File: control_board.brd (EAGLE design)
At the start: 190 x 180 mm, 132 parts, among them J17 JST_PH_B3B-PH-K-S(LF)(SN), J18 JST_PH_B3B-PH-K-S(LF)(SN), J19 JST_PH_B3B-PH-K-S(LF)(SN), J20 JST_PH_B3B-PH-K-S(LF)(SN), J21 JST_PH_B3B-PH-K-S(LF)(SN), J22 JST_PH_B3B-PH-K-S(LF)(SN), J23 JST_PH_B3B-PH-K-S(LF)(SN), J24 JST_PH_B3B-PH-K-S(LF)(SN), J25 JST_PH_B3B-PH-K-S(LF)(SN), J26 JST_PH_B3B-PH-K-S(LF)(SN), J27 JST_PH_B3B-PH-K-S(LF)(SN), J28 JST_PH_B3B-PH-K-S(LF)(SN), J29 JST_PH_B3B-PH-K-S(LF)(SN), J30 JST_PH_B3B-PH-K-S(LF)(SN), J31 JST_PH_B3B-PH-K-S(LF)(SN), J32 JST_PH_B3B-PH-K-S(LF)(SN), U18 AD7730BRUZ, U19 AD5360BSTZ, U20 ADR425ARZ, U21 AD7730BRUZ, U23 AD7730BRUZ, U24 AD7730BRUZ, U25 AD7730BRUZ, U26 AD7730BRUZ, U27 AD7730BRUZ, U28 AD7730BRUZ, U4 ADR421ARZ, U5 AD7616BSTZ, X1 22-23-2031, Y1 KC2520B-C1, Y3 KC2520B-C1

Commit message: rev 0.1
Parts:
- moved JP2 0.65 mm to (138.9, 1.30)
- moved JP3 0.65 mm to (22.1, 1.30)
- moved JP4 0.65 mm to (68.9, 1.30)
- moved JP6 0.65 mm to (5.85, 1.30)
- moved JP7 0.65 mm to (52.6, 1.30)
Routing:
- net DAC2_9: track 45.2 -> 45.8 mm
- net DAC2_8: track 46.5 -> 47.1 mm
- net DAC2_7: track 54.2 -> 54.9 mm
- net DAC2_6: track 50.8 -> 51.5 mm
- net DAC2_15: track 38.4 -> 39.1 mm
- net DAC2_1: track 41.0 -> 41.6 mm
- net ADC2_5: track 41.6 -> 42.2 mm
- net ADC2_10: track 57.2 -> 57.9 mm
- net DAC2_5: track 46.9 -> 47.5 mm
- net DAC2_4: track 43.4 -> 44.1 mm
- net DAC2_3: track 41.8 -> 42.5 mm
- net DAC2_2: track 40.7 -> 41.3 mm
- net DAC2_14: track 38.3 -> 38.9 mm
- net DAC2_13: track 39.6 -> 40.3 mm
- net DAC2_12: track 40.9 -> 41.6 mm
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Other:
- board text added: "Controller Board Hitzmann 2020"

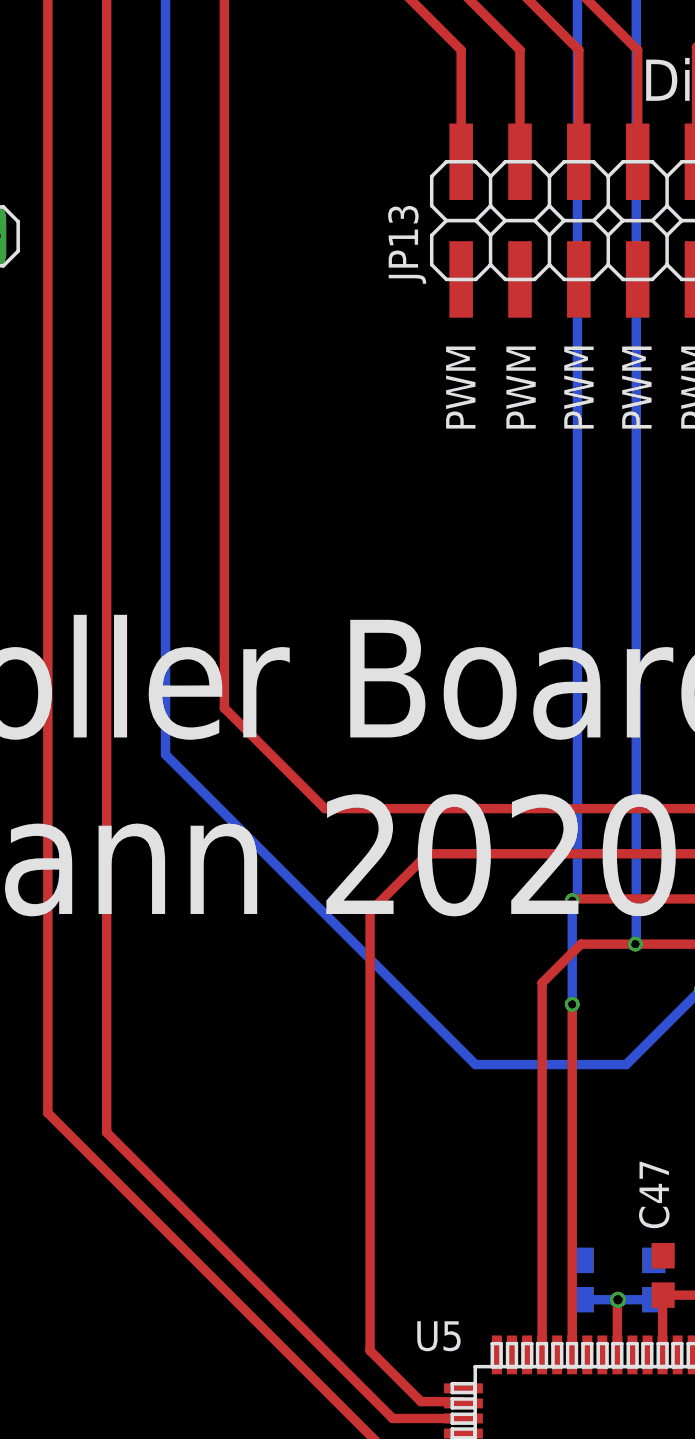
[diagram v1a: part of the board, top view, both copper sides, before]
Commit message: added GND to Teensy
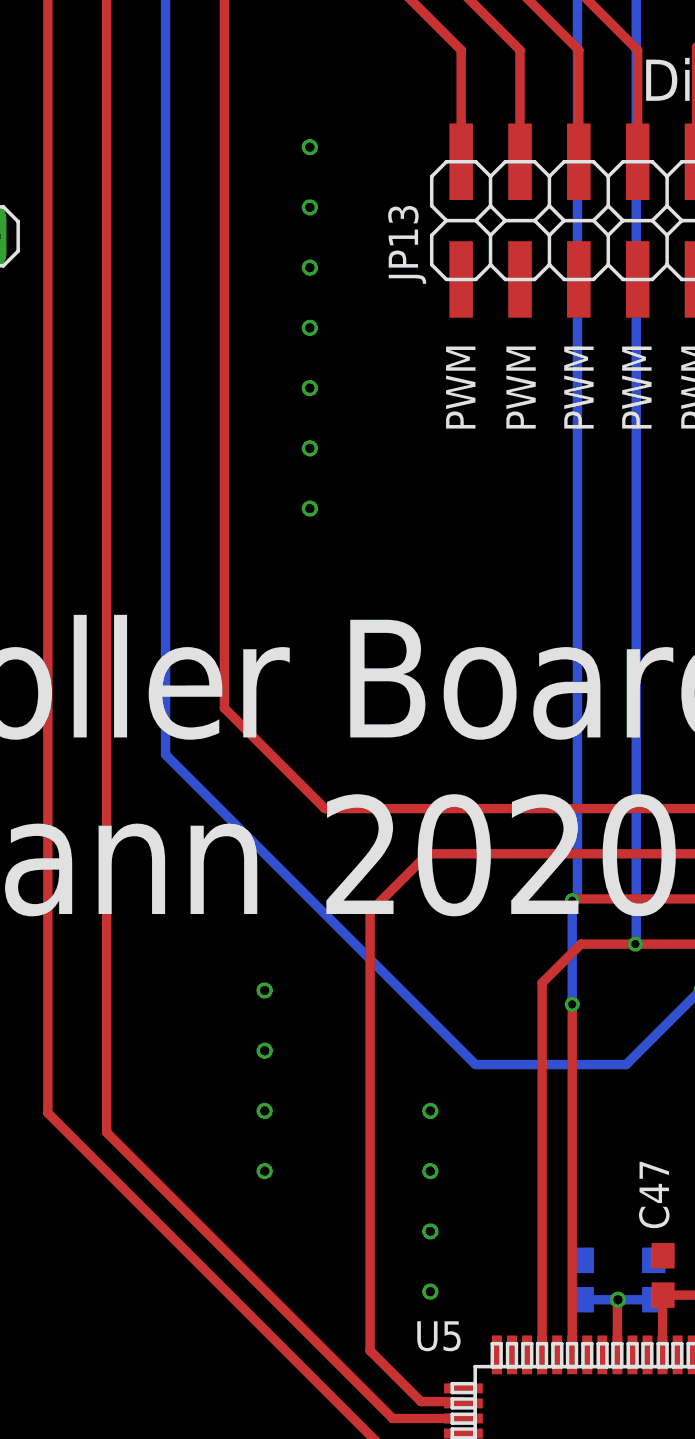
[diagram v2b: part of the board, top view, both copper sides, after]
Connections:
- net GND: now also U$1.GND1, U$1.GND3, U$1.GND6
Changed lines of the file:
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@@
 <via x="155.95" y="148.2" extent="1-16" drill="0.4"/>
 <via x="153.35" y="148.2" extent="1-16" drill="0.4"/>
+<via x="28.6" y="109.8" extent="1-16" drill="0.4"/>
+<via x="28.6" y="104.6" extent="1-16" drill="0.4"/>
+<via x="28.6" y="107.2" extent="1-16" drill="0.4"/>
+<via x="28.6" y="102" extent="1-16" drill="0.4"/>
+<via x="28.6" y="99.4" extent="1-16" drill="0.4"/>
+<via x="28.6" y="96.8" extent="1-16" drill="0.4"/>
+<via x="28.6" y="94.2" extent="1-16" drill="0.4"/>
+<via x="26.65" y="73.4" extent="1-16" drill="0.4"/>
+<via x="26.65" y="70.8" extent="1-16" drill="0.4"/>
+<via x="26.65" y="68.2" extent="1-16" drill="0.4"/>
+<via x="26.65" y="65.6" extent="1-16" drill="0.4"/>
+<via x="33.8" y="68.2" extent="1-16" drill="0.4"/>
+<via x="33.8" y="65.6" extent="1-16" drill="0.4"/>
+<via x="33.8" y="63" extent="1-16" drill="0.4"/>
+<via x="33.8" y="60.4" extent="1-16" drill="0.4"/>
+<contactref element="U$1" pad="GND1"/>
+<contactref element="U$1" pad="GND3"/>
+<contactref element="U$1" pad="GND6"/>
 </signal>
 <signal name="MISO">

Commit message: added caps and logo to control board
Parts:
- removed JP1: (no value), jumper:JP1
- added C12, C13, C14, C15, C16, C8: 100uF, rcl:E3,5-8
- moved LED1 15.6 mm to (12.3, 141.1)
- moved R11 15.1 mm to (17.6, 141.1)
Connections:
- removed net RPI_PWR: JP1.2, SV1.2, SV1.4
- removed net TEENSY_VIN: JP9.1, U$1.VIN
- new net PWR: C15.+, JP9.1, SV1.2, SV1.4, U$1.VIN
- net +5V: now also C13.+; no longer JP1.1
- net DVCC: now also C14.+
- net GND: now also C12.-, C13.-, C14.-, C15.-, C16.+, C8.-
- net VDD: now also C12.+, C8.+
- net VSS: now also C16.-
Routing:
- net PWR: track 0.00 -> 42.9 mm
- net VDD: track 690.7 -> 705.4 mm
- net HEARTBEAT: track 56.4 -> 43.1 mm
- net TEENSY_VIN: track 9.22 -> 0.00 mm
- net RPI_PWR: track 7.92 -> 0.00 mm
- net VSS: track 424.4 -> 427.8 mm
- net HB_CURR_LIM: track 4.05 -> 3.55 mm
